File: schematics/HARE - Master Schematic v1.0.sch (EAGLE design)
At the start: 97 parts, among them IC1 NE5532N, IC2 NE5532N, IC3 FT232RL, IC4 NE5532N, IC5 7805DT, IC6 AT25P, J1 9V, J2 STEREOSW, J3 STEREOSW, Q1 16 MHz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

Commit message: PWM-to-DC converter added for VCA control, VCF changes fixed, and fuse added
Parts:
- removed R26: 1k, resistor:R-US_R0805
- added C30: 22uF, gm-caps-electro-pol:0501
- added C31, C32: 470nF, gm-caps-film-box:072X0352
- added C33, C34: 0.1uF, resistor:C-EUC0805K
- added C35: .1uF, resistor:C-EUC0805K
- added F1: FUSELITTLEFUSE, fuse:FUSELITTLEFUSE
- added R34, R39: 1k, resistor:R-US_R0805
- D3: value LED5MM -> AMPLITUDE
- D4: value LED5MM -> CUTOFF
- D5: value LED5MM -> RESONANCE
- LDR1: value 100k -> CUTOFF
- LDR2: value 100k -> RESONANCE
- LDR3: value 100k -> AMPLITUDE
- R27: value 2.2k -> 1k
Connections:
- removed net N$60: R26.2, U1.PD3
- removed net N$61: D3.A, R26.1
- new net +5V1: C33.2, U1.AREF
- new net N$15: C30.+, IC1A.-IN, R34.2, R39.1
- new net N$19: D3.A, IC1A.OUT, R39.2
- new net N$34: C9.2, F1.2, IC5.VI
- new net PWM_DC: R34.1, U1.PD3
- net +5V: now also C16.1, C34.2, IC1P.V+; no longer U1.AREF
- net GND: now also C30.-, C31.2, C32.2, C33.1, C34.1, C35.1
- net N$57: now also C31.1
- net N$59: now also C32.1
- net VCC: now also F1.1; no longer C16.1, C9.2, IC1P.V+, IC5.VI
- net V_BIAS: now also C35.2, IC1A.+IN
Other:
- note added: "PWM to DC Converter (VCA Control)"
- note added: "The H.A.R.E Project - ECE411 Team 13"
- note removed: "The H.A.R.E Project - ECE411"
- moved on the sheet: C16, C19, C23, C3, C9, D3, D4, D5, IC5, LDR3, R27, R28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

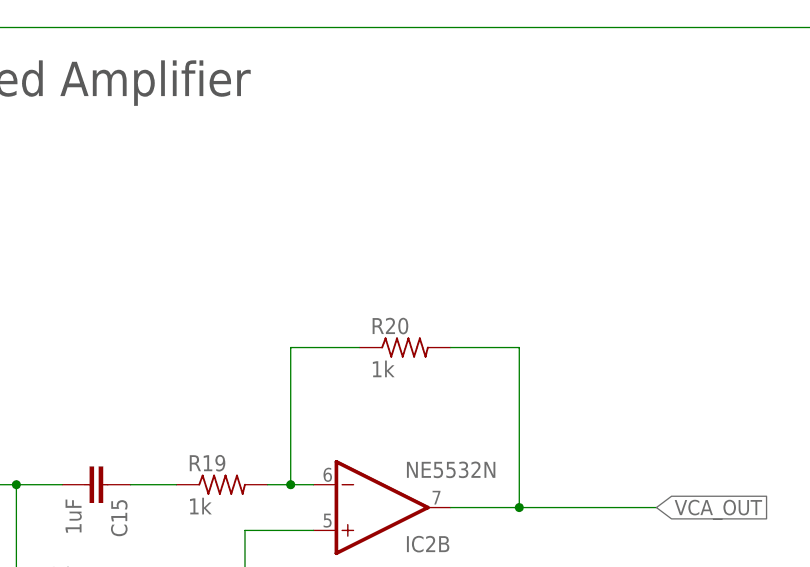
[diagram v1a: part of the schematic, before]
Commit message: Added filtering cap to analog output circuitry
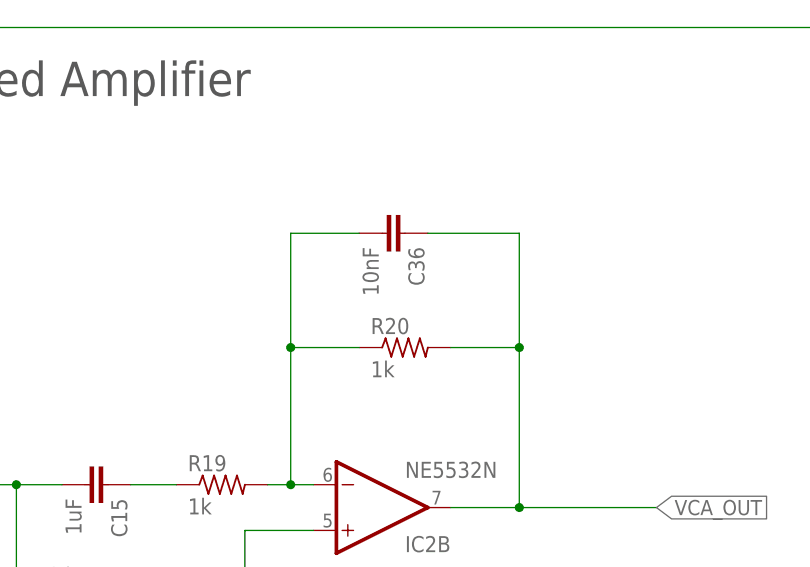
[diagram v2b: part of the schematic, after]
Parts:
- added C36: 10nF, resistor:C-EUC0805K
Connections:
- net N$33: now also C36.2
- net VCA_OUT: now also C36.1
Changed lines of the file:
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@@
 <part name="C35" library="resistor" library_urn="urn:adsk.eagle:library:348" deviceset="C-EU" device="C0805K" package3d_urn="urn:adsk.eagle:package:26201/1" value=".1uF"/>
 <part name="F1" library="fuse" deviceset="FUSE" device="LITTLEFUSE"/>
+<part name="C36" library="resistor" library_urn="urn:adsk.eagle:library:348" deviceset="C-EU" device="C0805K" package3d_urn="urn:adsk.eagle:package:26201/1" value="10nF"/>
 </parts>
 <sheets>
@@
 <instance part="C35" gate="G$1" x="447.04" y="368.3" rot="R180"/>
 <instance part="F1" gate="G$1" x="401.32" y="332.74"/>
+<instance part="C36" gate="G$1" x="111.76" y="152.4" rot="R270"/>
 </instances>
 <busses>
@@
 <pinref part="R20" gate="G$1" pin="1"/>
 <wire x1="99.06" y1="139.7" x2="106.68" y2="139.7" width="0.1524" layer="91"/>
+<wire x1="99.06" y1="139.7" x2="99.06" y2="152.4" width="0.1524" layer="91"/>
+<junction x="99.06" y="139.7"/>
+<pinref part="C36" gate="G$1" pin="2"/>
+<wire x1="99.06" y1="152.4" x2="106.68" y2="152.4" width="0.1524" layer="91"/>
 </segment>
 </net>
@@
 <junction x="124.46" y="121.92"/>
 <wire x1="124.46" y1="121.92" x2="139.7" y2="121.92" width="0.1524" layer="91"/>
-</segment>
-<segment>
+<pinref part="C36" gate="G$1" pin="1"/>
+<wire x1="114.3" y1="152.4" x2="124.46" y2="152.4" width="0.1524" layer="91"/>
+<wire x1="124.46" y1="152.4" x2="124.46" y2="139.7" width="0.1524" layer="91"/>
+<junction x="124.46" y="139.7"/>
+</segment>
+<segment>

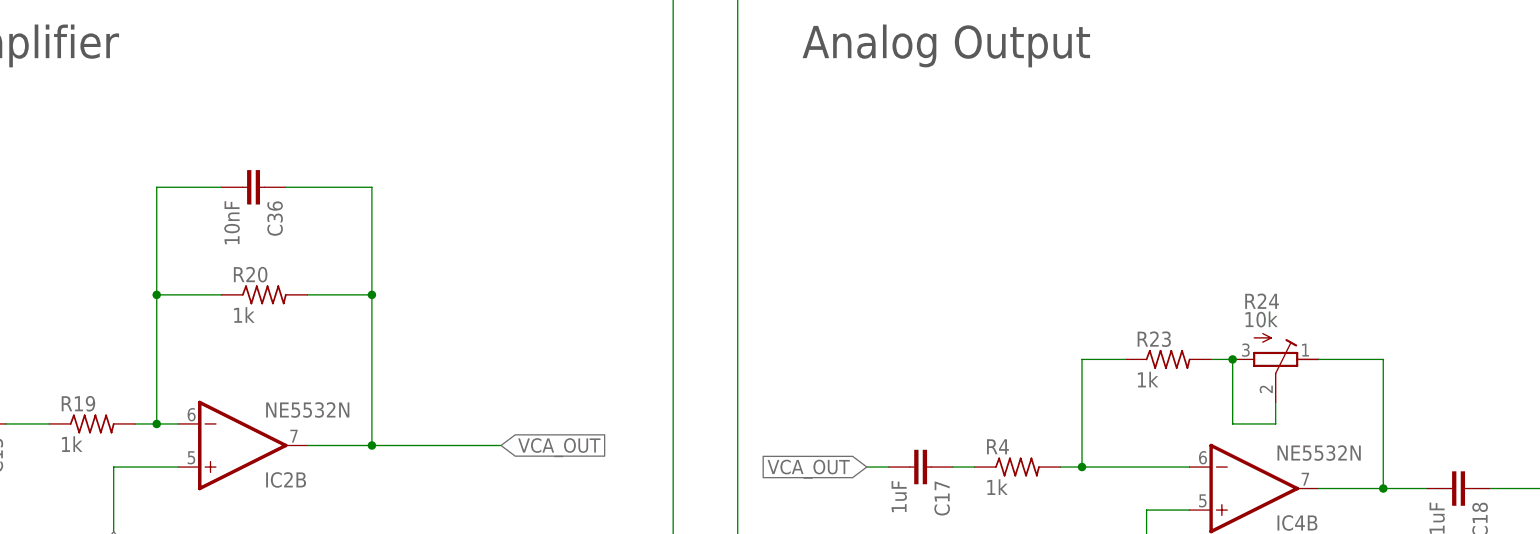
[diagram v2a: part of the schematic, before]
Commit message: Added high frequency filter cap to analog output circuitry
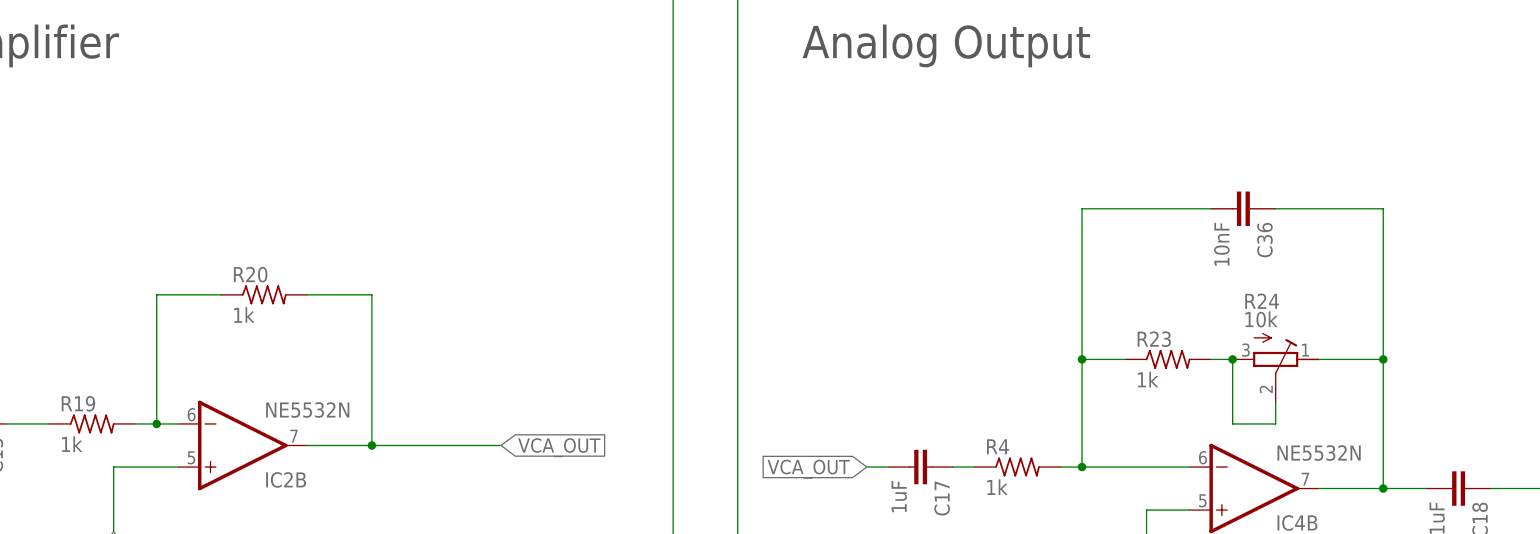
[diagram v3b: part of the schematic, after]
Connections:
- net N$33: no longer C36.2
- net N$41: now also C36.2
- net N$43: now also C36.1
- net VCA_OUT: no longer C36.1
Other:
- moved on the sheet: C36
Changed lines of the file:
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@@
 <instance part="C35" gate="G$1" x="447.04" y="368.3" rot="R180"/>
 <instance part="F1" gate="G$1" x="401.32" y="332.74"/>
-<instance part="C36" gate="G$1" x="111.76" y="152.4" rot="R270"/>
+<instance part="C36" gate="G$1" x="228.6" y="149.86" rot="R270"/>
 </instances>
 <busses>
@@
 <pinref part="R20" gate="G$1" pin="1"/>
 <wire x1="99.06" y1="139.7" x2="106.68" y2="139.7" width="0.1524" layer="91"/>
-<wire x1="99.06" y1="139.7" x2="99.06" y2="152.4" width="0.1524" layer="91"/>
-<junction x="99.06" y="139.7"/>
-<pinref part="C36" gate="G$1" pin="2"/>
-<wire x1="99.06" y1="152.4" x2="106.68" y2="152.4" width="0.1524" layer="91"/>
 </segment>
 </net>
@@
 <junction x="124.46" y="121.92"/>
 <wire x1="124.46" y1="121.92" x2="139.7" y2="121.92" width="0.1524" layer="91"/>
-<pinref part="C36" gate="G$1" pin="1"/>
-<wire x1="114.3" y1="152.4" x2="124.46" y2="152.4" width="0.1524" layer="91"/>
-<wire x1="124.46" y1="152.4" x2="124.46" y2="139.7" width="0.1524" layer="91"/>
-<junction x="124.46" y="139.7"/>
 </segment>
 <segment>
@@
 <pinref part="R23" gate="G$1" pin="1"/>
 <wire x1="208.28" y1="132.08" x2="213.36" y2="132.08" width="0.1524" layer="91"/>
+<wire x1="208.28" y1="132.08" x2="208.28" y2="149.86" width="0.1524" layer="91"/>
+<junction x="208.28" y="132.08"/>
+<pinref part="C36" gate="G$1" pin="2"/>
+<wire x1="208.28" y1="149.86" x2="223.52" y2="149.86" width="0.1524" layer="91"/>
 </segment>
 </net>
@@
 <wire x1="243.84" y1="116.84" x2="248.92" y2="116.84" width="0.1524" layer="91"/>
 <junction x="243.84" y="116.84"/>
-</segment>
-</net>
+<pinref part="C36" gate="G$1" pin="1"/>
+<wire x1="231.14" y1="149.86" x2="243.84" y2="149.86" width="0.1524" layer="91"/>
+<wire x1="243.84" y1="149.86" x2="243.84" y2="132.08" width="0.1524" layer="91"/>
+<junction x="243.84" y="132.08"/>
+</segment>
+</net>

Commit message: new chip and bootloader
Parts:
- removed IC6: AT25P, atmel:AT25P
- added C37: 10uF, resistor:C-EUC0805K
- added IC7: TM1804IS62/65WVS0648, IS62-65WVS0648:TM1804IS62/65WVS0648
- added R26: 10k, rcl:R-US_M0805
- added R40: 1k, resistor:R-US_R0805
- R37: value 1k -> 10k
- R8: value 10k -> 1k; device rcl:R-US_M0805 -> resistor:R-US_R0805
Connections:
- removed net N$24: IC3.!DCD, IC3.!DSR, IC3.!DTR, IC3.!RI, R37.2
- removed net N$8: IC6.HOLD/, R7.2
- new net DELEETE: IC3.!DCD, IC3.!DSR, IC3.!RI, R37.2
- new net ISP_DTR: C28.2, IC3.!DTR
- new net N$35: IC7.HLD/, R26.1
- new net N$38: R8.2, U1.PD0
- new net N$44: IC7.DNU, R7.2
- net +5V: now also C37.2, IC7.VDD, R26.2, R37.1; no longer C28.2, IC6.VCC, R8.1
- net GND: now also C37.1, IC7.VSS; no longer C28.1, IC6.GND, R37.1
- net MEM_CS: now also IC7.CS/; no longer IC6.CS/
- net N$18: now also R40.2, U1.PD1; no longer IC6.WP/, R8.2
- net N$28: now also IC3.OSCO
- net RESET#: now also C28.1
- net RXD: now also R8.1; no longer U1.PD0
- net SPI_MISO: now also IC7.SO; no longer IC6.SO
- net SPI_MOSI: now also IC7.SI, U1.PB3; no longer IC6.SI, U1.PB5
- net SPI_SCK: now also IC7.SCK, U1.PB5; no longer IC6.SCK, U1.PB3
- net TXD: now also R40.1; no longer U1.PD1
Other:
- note added: "BootLoader Connections"
- moved on the sheet: C28, R37, R38, R7, R8, R9

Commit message: Finished Board layout without art
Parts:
- removed IC7: TM1804IS62/65WVS0648, IS62-65WVS0648:TM1804IS62/65WVS0648
- added IC6: TM1804IS62/65WVS0648, IS62-65WVS0648:TM1804IS62/65WVS0648
- R26: value 10k -> 1k; device rcl:R-US_M0805 -> resistor:R-US_R0805
- R8: value 1k -> 10k; device resistor:R-US_R0805 -> rcl:R-US_M0805
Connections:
- net DELEETE renamed N$24
- removed net N$38 (its old number): R8.2, U1.PD0
- removed net N$44: IC7.DNU, R7.2
- new net N$18: IC6.DNU, R8.2
- new net N$8: IC6.HLD/, R9.2
- net +5V: now also C28.2, IC6.VDD, R8.1; no longer C37.2, IC7.VDD, R26.2
- net GND: now also C28.1, IC6.VSS; no longer C37.1, IC7.VSS
- net ISP_DTR: now also C37.1; no longer C28.2
- net MEM_CS: now also IC6.CS/, R7.2; no longer IC7.CS/, R9.2
- net N$35: now also R26.2, U1.PD0; no longer IC7.HLD/, R26.1
- net RESET#: now also C37.2; no longer C28.1
- net RXD: now also R26.1; no longer R8.1
- net SPI_MISO: now also IC6.SO; no longer IC7.SO
- net SPI_MOSI: now also IC6.SI; no longer IC7.SI
- net SPI_SCK: now also IC6.SCK; no longer IC7.SCK
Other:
- note removed: "BootLoader Connections"
- moved on the sheet: C28, C37, R26, R37, R38, R7, R8, R9

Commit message: REV 1 for HARE ready for tapeout
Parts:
- added R41, R42, R43, R44, R45: 10k, resistor:R-US_R0805
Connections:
- new net N$39: R41.2, U1.PB0
- new net N$44: R42.2, U1.PB1
- new net N$47: R43.2, U1.PB2
- new net N$50: R44.1, U1.PC4
- new net N$55: R45.1, U1.PC5
- net GND: now also R41.1, R42.1, R43.1, R44.2, R45.2, U1.GND
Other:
- moved on the sheet: C33
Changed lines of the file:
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@@
 <part name="R40" library="resistor" library_urn="urn:adsk.eagle:library:348" deviceset="R-US_" device="R0805" package3d_urn="urn:adsk.eagle:package:26059/1" value="1k"/>
 <part name="C37" library="resistor" library_urn="urn:adsk.eagle:library:348" deviceset="C-EU" device="C0805K" package3d_urn="urn:adsk.eagle:package:26201/1" value="10uF"/>
+<part name="R41" library="resistor" library_urn="urn:adsk.eagle:library:348" deviceset="R-US_" device="R0805" package3d_urn="urn:adsk.eagle:package:26059/1" value="10k"/>
+<part name="R42" library="resistor" library_urn="urn:adsk.eagle:library:348" deviceset="R-US_" device="R0805" package3d_urn="urn:adsk.eagle:package:26059/1" value="10k"/>
+<part name="R43" library="resistor" library_urn="urn:adsk.eagle:library:348" deviceset="R-US_" device="R0805" package3d_urn="urn:adsk.eagle:package:26059/1" value="10k"/>
+<part name="R44" library="resistor" library_urn="urn:adsk.eagle:library:348" deviceset="R-US_" device="R0805" package3d_urn="urn:adsk.eagle:package:26059/1" value="10k"/>
+<part name="R45" library="resistor" library_urn="urn:adsk.eagle:library:348" deviceset="R-US_" device="R0805" package3d_urn="urn:adsk.eagle:package:26059/1" value="10k"/>
 </parts>
 <sheets>
@@
 <instance part="C31" gate="G$1" x="129.54" y="314.96"/>
 <instance part="C32" gate="G$1" x="147.32" y="314.96"/>
-<instance part="C33" gate="G$1" x="60.96" y="340.36" rot="R180"/>
+<instance part="C33" gate="G$1" x="55.88" y="342.9" rot="R180"/>
 <instance part="SUPPLY47" gate="GND" x="60.96" y="332.74"/>
 <instance part="C34" gate="G$1" x="71.12" y="358.14" rot="R180"/>
@@
 <instance part="R40" gate="G$1" x="132.08" y="353.06" rot="R180"/>
 <instance part="C37" gate="G$1" x="137.16" y="383.54" rot="R180"/>
+<instance part="R41" gate="G$1" x="71.12" y="342.9"/>
+<instance part="R42" gate="G$1" x="71.12" y="340.36"/>
+<instance part="R43" gate="G$1" x="71.12" y="337.82"/>
+<instance part="R44" gate="G$1" x="121.92" y="322.58"/>
+<instance part="R45" gate="G$1" x="121.92" y="320.04"/>
 </instances>
 <busses>
@@
 <pinref part="U1" gate="A" pin="GND_2"/>
 <wire x1="78.74" y1="320.04" x2="66.04" y2="320.04" width="0.1524" layer="91"/>
-<wire x1="66.04" y1="320.04" x2="66.04" y2="312.42" width="0.1524" layer="91"/>
+<wire x1="66.04" y1="320.04" x2="66.04" y2="317.5" width="0.1524" layer="91"/>
+<wire x1="66.04" y1="317.5" x2="66.04" y2="312.42" width="0.1524" layer="91"/>
 <wire x1="66.04" y1="312.42" x2="25.4" y2="312.42" width="0.1524" layer="91"/>
 <junction x="25.4" y="312.42"/>
+<pinref part="U1" gate="A" pin="GND"/>
+<wire x1="78.74" y1="317.5" x2="66.04" y2="317.5" width="0.1524" layer="91"/>
+<junction x="66.04" y="317.5"/>
 </segment>
 <segment>
@@
 <pinref part="C31" gate="G$1" pin="2"/>
 <pinref part="SUPPLY46" gate="GND" pin="GND"/>
-<wire x1="129.54" y1="312.42" x2="129.54" y2="299.72" width="0.1524" layer="91"/>
+<wire x1="129.54" y1="312.42" x2="129.54" y2="302.26" width="0.1524" layer="91"/>
+<wire x1="129.54" y1="302.26" x2="129.54" y2="299.72" width="0.1524" layer="91"/>
+<wire x1="127" y1="322.58" x2="127" y2="320.04" width="0.1524" layer="91"/>
+<wire x1="127" y1="320.04" x2="127" y2="302.26" width="0.1524" layer="91"/>
+<wire x1="127" y1="302.26" x2="129.54" y2="302.26" width="0.1524" layer="91"/>
+<junction x="129.54" y="302.26"/>
+<pinref part="R44" gate="G$1" pin="2"/>
+<pinref part="R45" gate="G$1" pin="2"/>
+<junction x="127" y="320.04"/>
 </segment>
 <segment>
@@
 <pinref part="C33" gate="G$1" pin="1"/>
 <wire x1="60.96" y1="335.28" x2="60.96" y2="337.82" width="0.1524" layer="91"/>
+<wire x1="60.96" y1="337.82" x2="60.96" y2="340.36" width="0.1524" layer="91"/>
+<wire x1="60.96" y1="340.36" x2="55.88" y2="340.36" width="0.1524" layer="91"/>
+<pinref part="R41" gate="G$1" pin="1"/>
+<wire x1="66.04" y1="342.9" x2="60.96" y2="342.9" width="0.1524" layer="91"/>
+<wire x1="60.96" y1="342.9" x2="60.96" y2="340.36" width="0.1524" layer="91"/>
+<junction x="60.96" y="340.36"/>
+<pinref part="R42" gate="G$1" pin="1"/>
+<wire x1="66.04" y1="340.36" x2="60.96" y2="340.36" width="0.1524" layer="91"/>
+<pinref part="R43" gate="G$1" pin="1"/>
+<wire x1="66.04" y1="337.82" x2="60.96" y2="337.82" width="0.1524" layer="91"/>
+<junction x="60.96" y="337.82"/>
 </segment>
 <segment>
@@
 <segment>
 <pinref part="C33" gate="G$1" pin="2"/>
-<wire x1="60.96" y1="345.44" x2="60.96" y2="347.98" width="0.1524" layer="91"/>
 <pinref part="U1" gate="A" pin="AREF"/>
-<wire x1="60.96" y1="347.98" x2="78.74" y2="347.98" width="0.1524" layer="91"/>
+<wire x1="55.88" y1="347.98" x2="78.74" y2="347.98" width="0.1524" layer="91"/>
 </segment>
 </net>
@@
 </segment>
 </net>
+<net name="N$39" class="0">
+<segment>
+<pinref part="U1" gate="A" pin="PB0"/>
+<pinref part="R41" gate="G$1" pin="2"/>
+<wire x1="78.74" y1="342.9" x2="76.2" y2="342.9" width="0.1524" layer="91"/>
+</segment>
+</net>
+<net name="N$44" class="0">
+<segment>
+<pinref part="U1" gate="A" pin="PB1"/>
+<pinref part="R42" gate="G$1" pin="2"/>
+<wire x1="78.74" y1="340.36" x2="76.2" y2="340.36" width="0.1524" layer="91"/>
+</segment>
+</net>
+<net name="N$47" class="0">
+<segment>
+<pinref part="U1" gate="A" pin="PB2"/>
+<pinref part="R43" gate="G$1" pin="2"/>
+<wire x1="78.74" y1="337.82" x2="76.2" y2="337.82" width="0.1524" layer="91"/>
+</segment>
+</net>
+<net name="N$50" class="0">
+<segment>
+<pinref part="U1" gate="A" pin="PC4"/>
+<pinref part="R44" gate="G$1" pin="1"/>
+<wire x1="116.84" y1="322.58" x2="114.3" y2="322.58" width="0.1524" layer="91"/>
+</segment>
+</net>
+<net name="N$55" class="0">
+<segment>
+<pinref part="U1" gate="A" pin="PC5"/>
+<pinref part="R45" gate="G$1" pin="1"/>
+<wire x1="116.84" y1="320.04" x2="114.3" y2="320.04" width="0.1524" layer="91"/>
+</segment>
+</net>
